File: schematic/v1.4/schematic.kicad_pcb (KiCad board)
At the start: 4 copper layers, 85.5 x 22.9 mm, 16 parts, among them J1 USB C Breakout, J2 PWR SW, Q1 AO3401, Q2 2N2222, U1 ESP32-C3, U2 4466, U5 WS2812B, U6 AMS1117

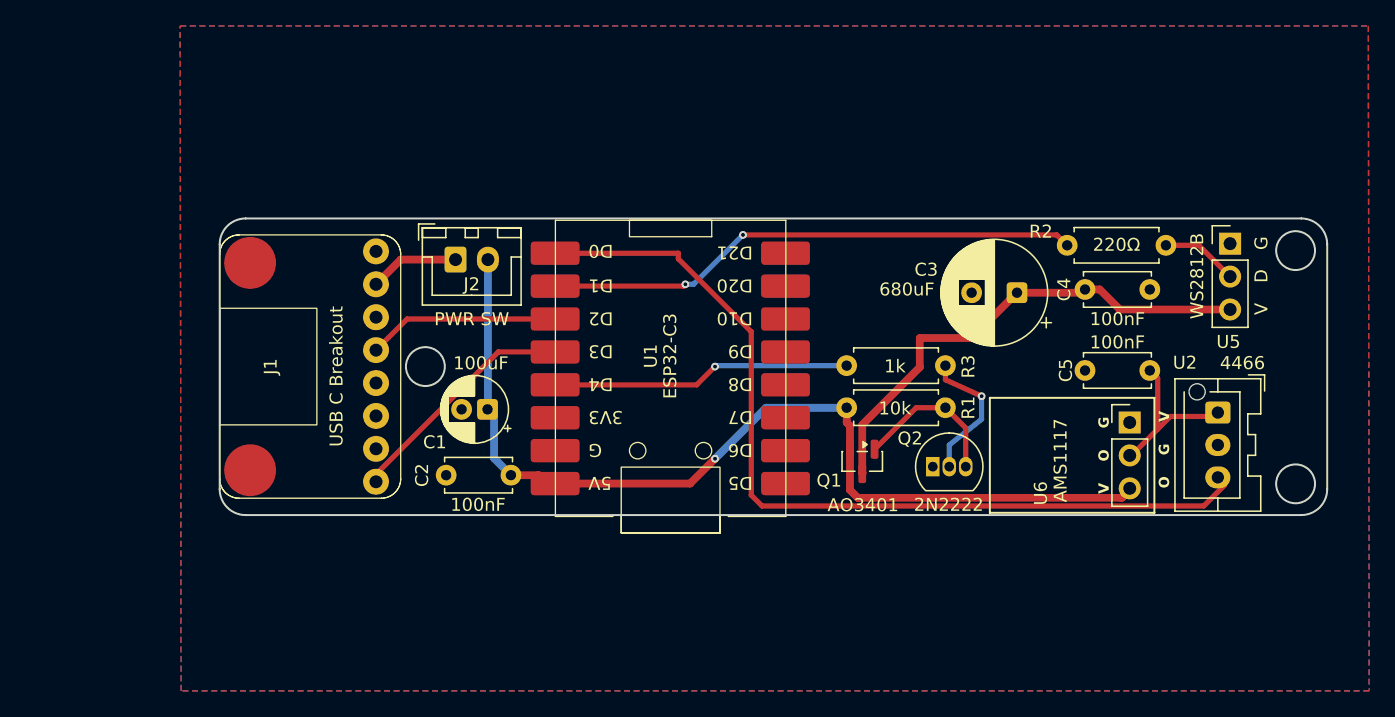
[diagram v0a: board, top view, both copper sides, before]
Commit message: Add support for usb c and a power communication with cutoff
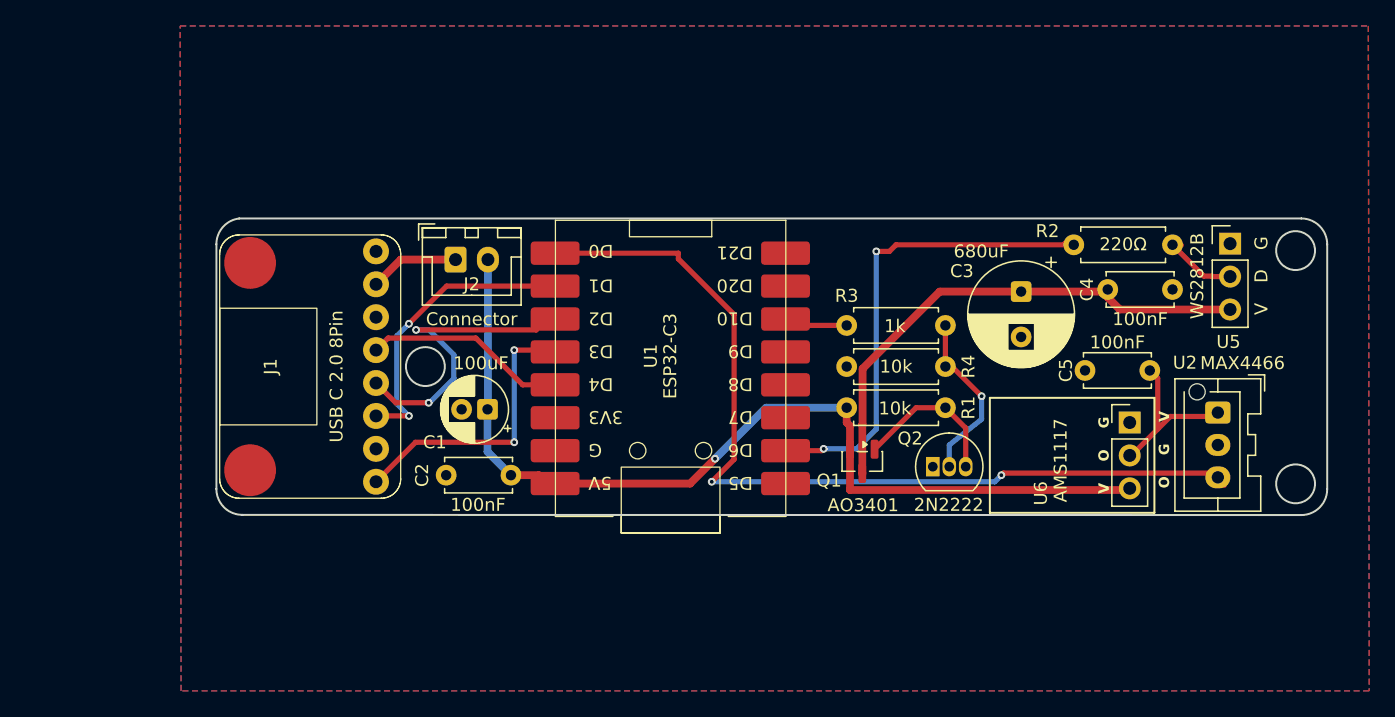
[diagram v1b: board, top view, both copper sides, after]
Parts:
- added R4: 10k, Resistor_THT:R_Axial_DIN0207_L6.3mm_D2.5mm_P7.62mm_Horizontal, F.Cu at (93.7, 44.5)
- J1: value USB C Breakout -> USB C 2.0 8Pin
- J2: value PWR SW -> Connector
- U2: value 4466 -> MAX4466
- moved R3 3.10 mm to (86.1, 41.3)
- moved C4 1.75 mm to (111.3, 38.5)
- moved R2 0.51 mm to (103.6, 35.1)
- moved C3 0.33 mm to (99.6, 38.7), turned to -90 degrees
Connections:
- J1 pad A6: unconnected-(J1-D+-PadA6) -> D+
- J1 pad A7: unconnected-(J1-D--PadA7) -> D-
- U1 pad 10: unconnected-(U1-D6-Pad10) -> LED D
- U1 pad 14: unconnected-(U1-D10-Pad14) -> LED SW
- U1 pad 4: LED SW -> CC1
- U1 pad 6: CC1 -> D-
- U1 pad 7: LED D -> D+
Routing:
- net D-: track 0.00 -> 23.4 mm, vias 0 -> 2
- net D+: track 0.00 -> 22.3 mm, vias 0 -> 2
- net LED SW: track 23.7 -> 7.27 mm, vias 1 -> 0
- net CC2: track 17.7 -> 23.1 mm, vias 0 -> 2
- net LED D: track 42.1 -> 38.2 mm
- net Net-(Q2-B): track 10.8 -> 13.6 mm
- net +5VD: track 38.5 -> 40.0 mm
- net MIC: track 69.5 -> 70.6 mm, vias 0 -> 2
- net +5V: track 74.6 -> 73.7 mm
- net CC1: track 14.2 -> 15.1 mm
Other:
- board size 85.5 x 22.9 mm -> 85.7 x 22.9 mm

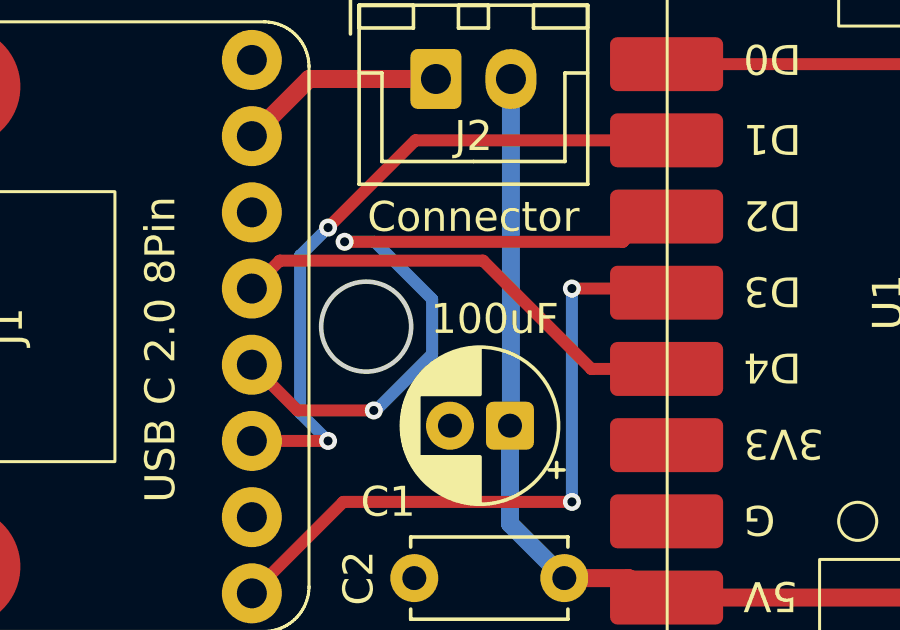
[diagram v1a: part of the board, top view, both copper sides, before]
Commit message: Add usb a power support
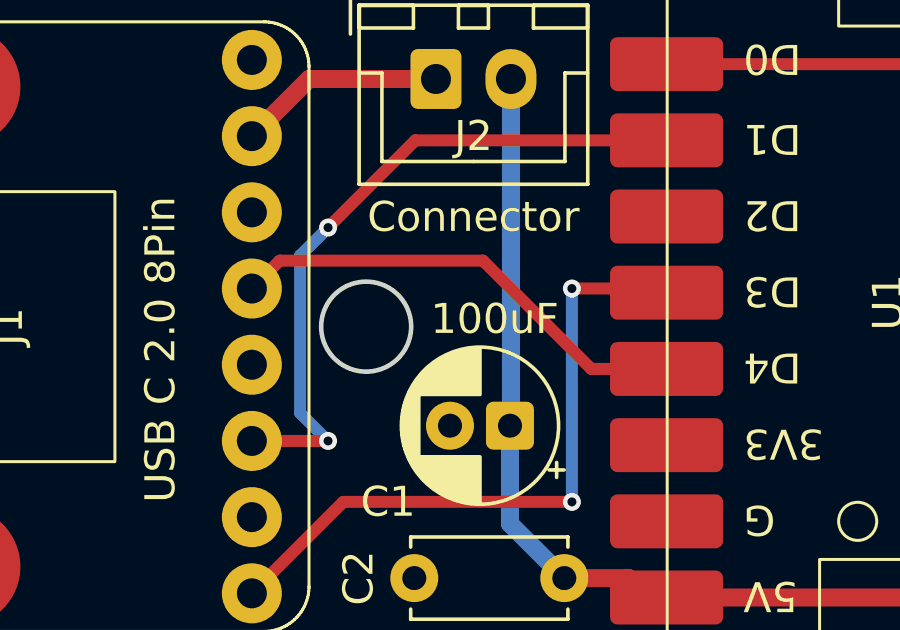
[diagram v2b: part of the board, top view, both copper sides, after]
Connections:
- J1 pad A7: D- -> Net-(J1-D--PadA7)
- U1 pad 6: D- -> unconnected-(U1-D2-Pad6)
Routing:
- net D-: track 23.4 -> 0.00 mm, vias 2 -> 0

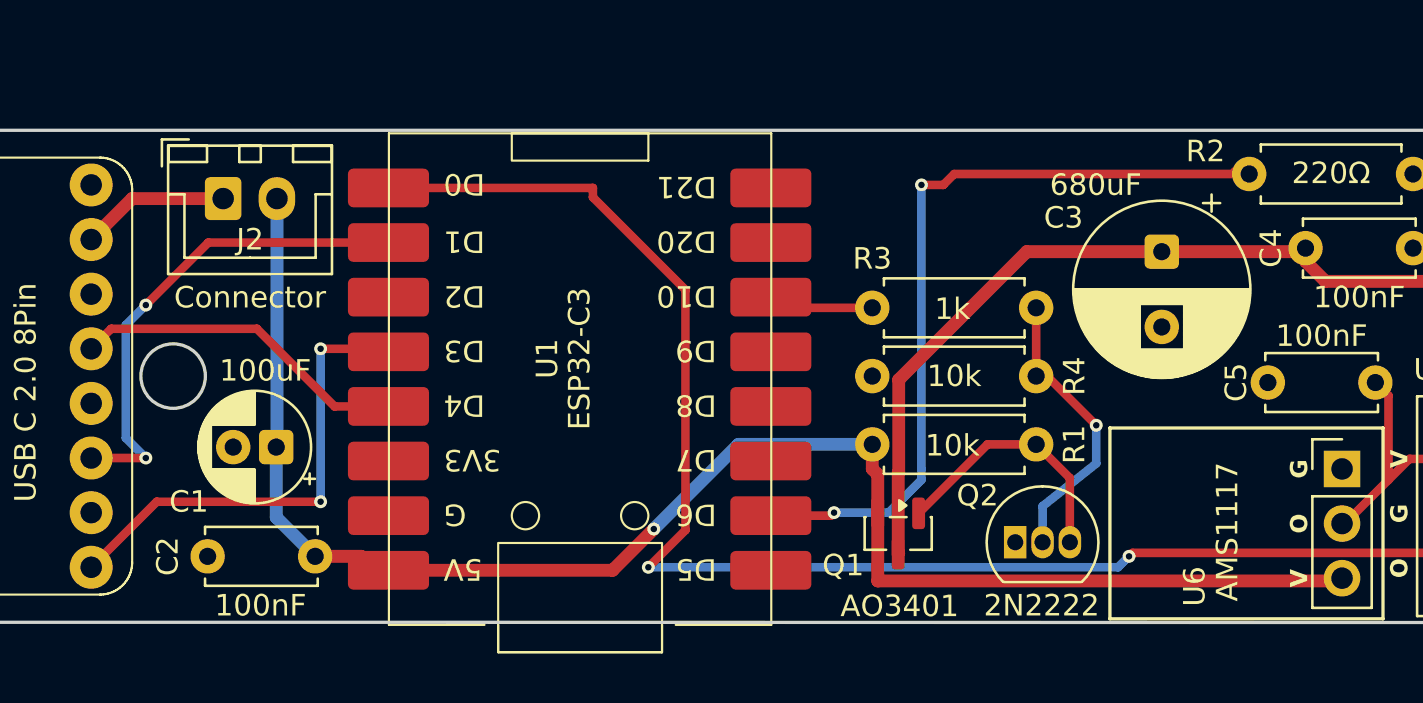
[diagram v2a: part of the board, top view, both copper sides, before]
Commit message: Add D+ pull up
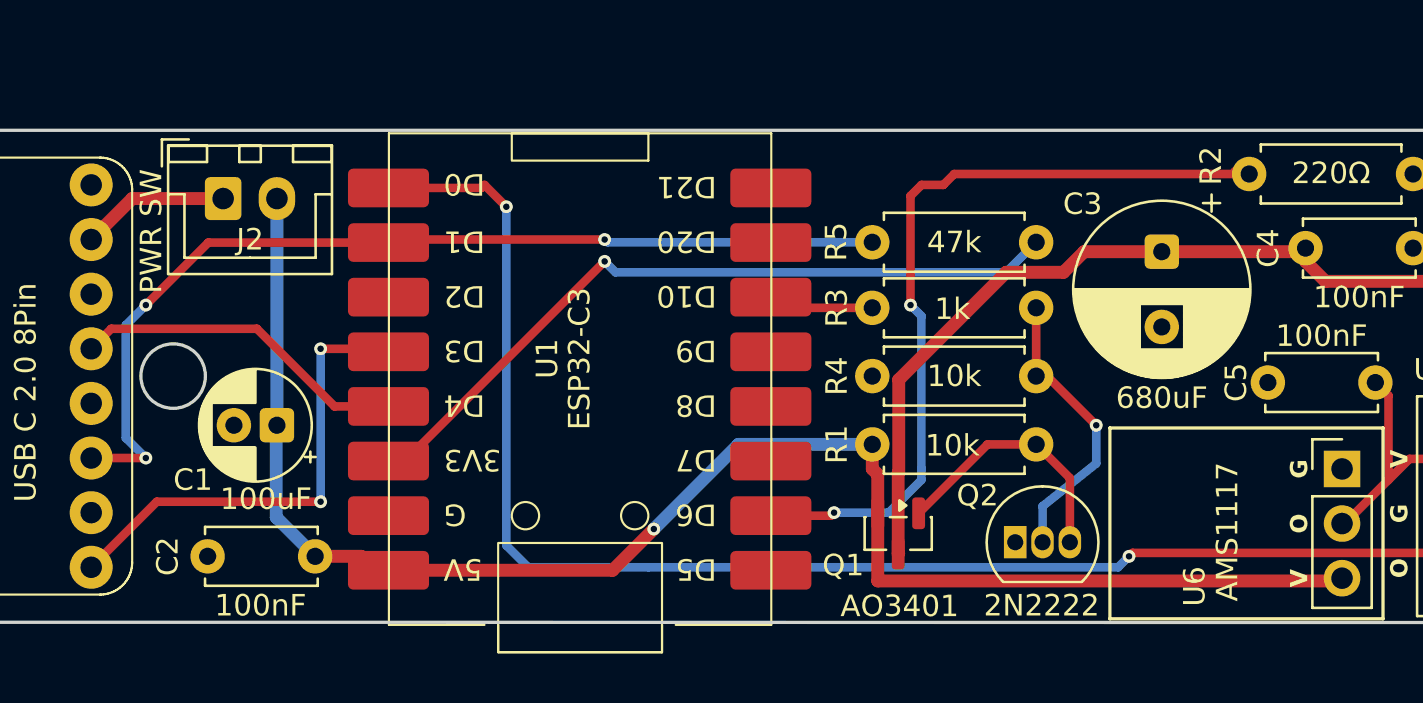
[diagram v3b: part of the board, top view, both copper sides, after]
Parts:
- added R5: 47k, Resistor_THT:R_Axial_DIN0207_L6.3mm_D2.5mm_P7.62mm_Horizontal, F.Cu at (86.1, 38.2)
- J2: value Connector -> PWR SW
- moved C1 1.02 mm to (58.4, 46.7)
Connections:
- U1 pad 3: unconnected-(U1-3V3-Pad3) -> +3.3V
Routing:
- net +3.3V: track 0.00 -> 35.4 mm, vias 0 -> 1
- net D+: track 22.3 -> 45.5 mm, vias 2 -> 3
- net +5V: track 73.7 -> 74.8 mm
- net MIC: track 70.6 -> 69.6 mm

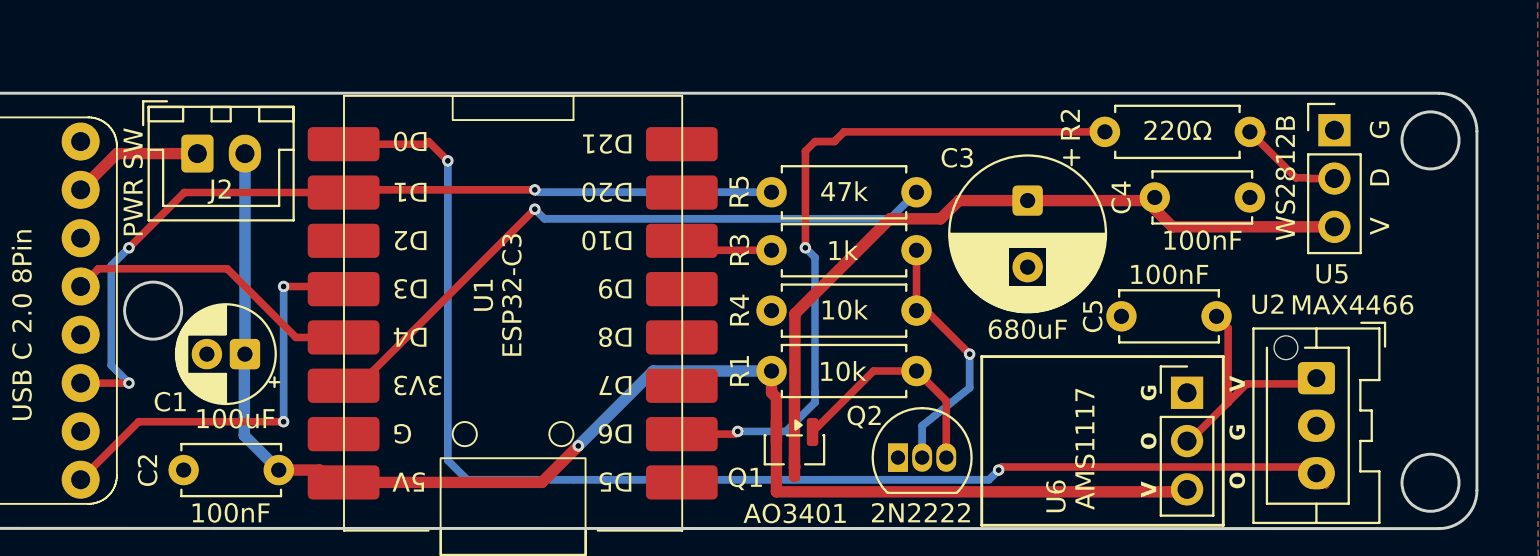
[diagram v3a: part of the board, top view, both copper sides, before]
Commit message: Adjust pcb and add icons to webserver
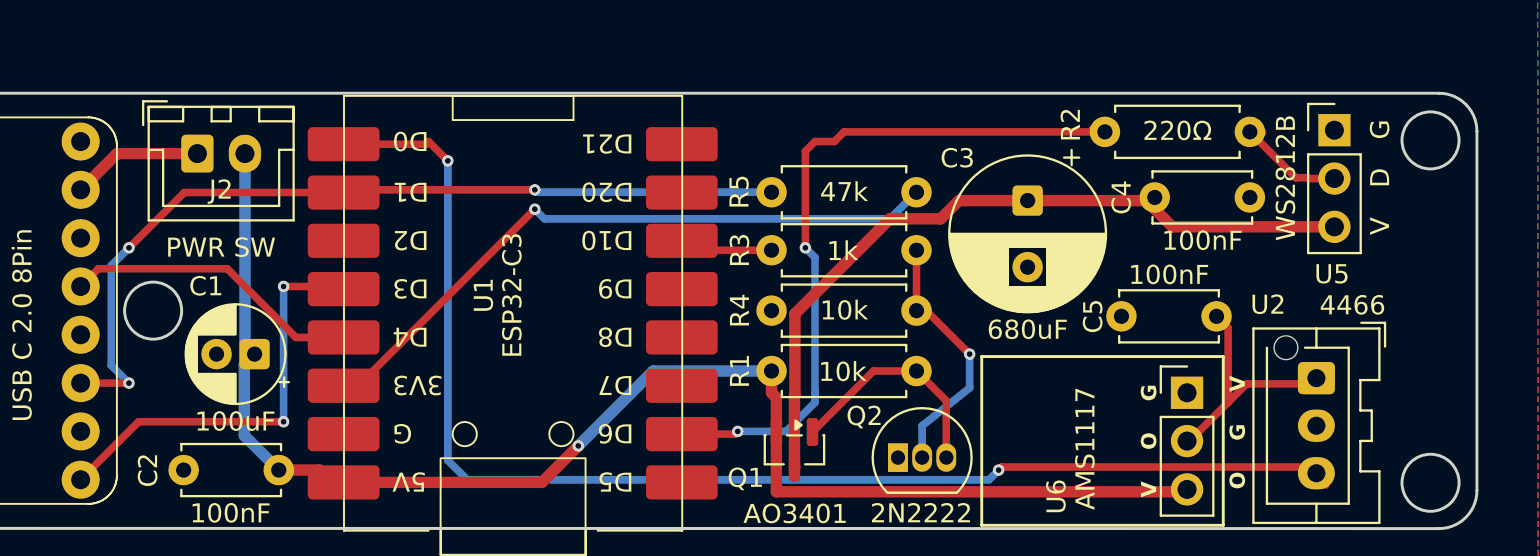
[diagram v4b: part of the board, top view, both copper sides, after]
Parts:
- U2: value MAX4466 -> 4466
- moved C1 0.51 mm to (58.9, 46.7)
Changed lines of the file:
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@@
 		)
 		(property "Value" "PWR SW"
-			(at -3.342 1.524 90)
+			(at 1.23 4.953 180)
 			(layer "F.SilkS")
 			(effects
@@
 			)
 		)
-		(property "Value" "MAX4466"
+		(property "Value" "4466"
 			(at -3.8185 -1.905 180)
 			(layer "F.SilkS")
@@
 	(footprint "Capacitor_THT:CP_Radial_D5.0mm_P2.00mm"
 		(layer "F.Cu")
-		(at 58.42 46.736 180)
+		(at 58.928 46.736 180)
 		(descr "CP, Radial series, Radial, pin pitch=2.00mm, diameter=5mm, height=7mm, Electrolytic Capacitor")
 		(tags "CP Radial series Radial pin pitch 2.00mm diameter 5mm height 7mm Electrolytic Capacitor")
 		(property "Reference" "C1"
-			(at 3.905 -2.54 0)
+			(at 2.54 3.556 0)
 			(layer "F.SilkS")
 			(effects
@@
 		)
 		(property "Value" "100uF"
-			(at 0.508 -3.429 0)
+			(at 1.016 -3.556 0)
 			(layer "F.SilkS")
 			(effects
@@
 	)
 	(segment
-		(start 58.388 47.276)
-		(end 58.388 51.022)
+		(start 58.42 36.195)
+		(end 58.42 47.276)
 		(width 0.6)
 		(layer "B.Cu")
@@
 	)
 	(segment
-		(start 58.42 47.244)
-		(end 58.388 47.276)
+		(start 58.388 51.022)
+		(end 60.198 52.832)
 		(width 0.6)
 		(layer "B.Cu")
@@
 	)
 	(segment
-		(start 58.42 36.195)
-		(end 58.42 47.276)
+		(start 58.928 46.736)
+		(end 58.388 47.276)
 		(width 0.6)
 		(layer "B.Cu")
@@
 	)
 	(segment
-		(start 79.883 47.625)
-		(end 86.106 47.625)
-		(width 0.6)
-		(layer "B.Cu")
-		(net 2)
-	)
-	(segment
-		(start 58.388 51.022)
-		(end 60.198 52.832)
+		(start 58.388 47.276)
+		(end 58.388 51.022)
 		(width 0.6)
 		(layer "B.Cu")
@@
 	)
 	(segment
-		(start 58.42 46.736)
-		(end 58.42 47.244)
+		(start 79.883 47.625)
+		(end 86.106 47.625)
 		(width 0.6)
 		(layer "B.Cu")
